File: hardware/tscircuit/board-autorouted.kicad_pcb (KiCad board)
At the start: 4 copper layers, 80 x 175 mm, 174 parts, among them SW1 10mΩ, SW11 10mΩ, SW12 10mΩ, SW13 10mΩ

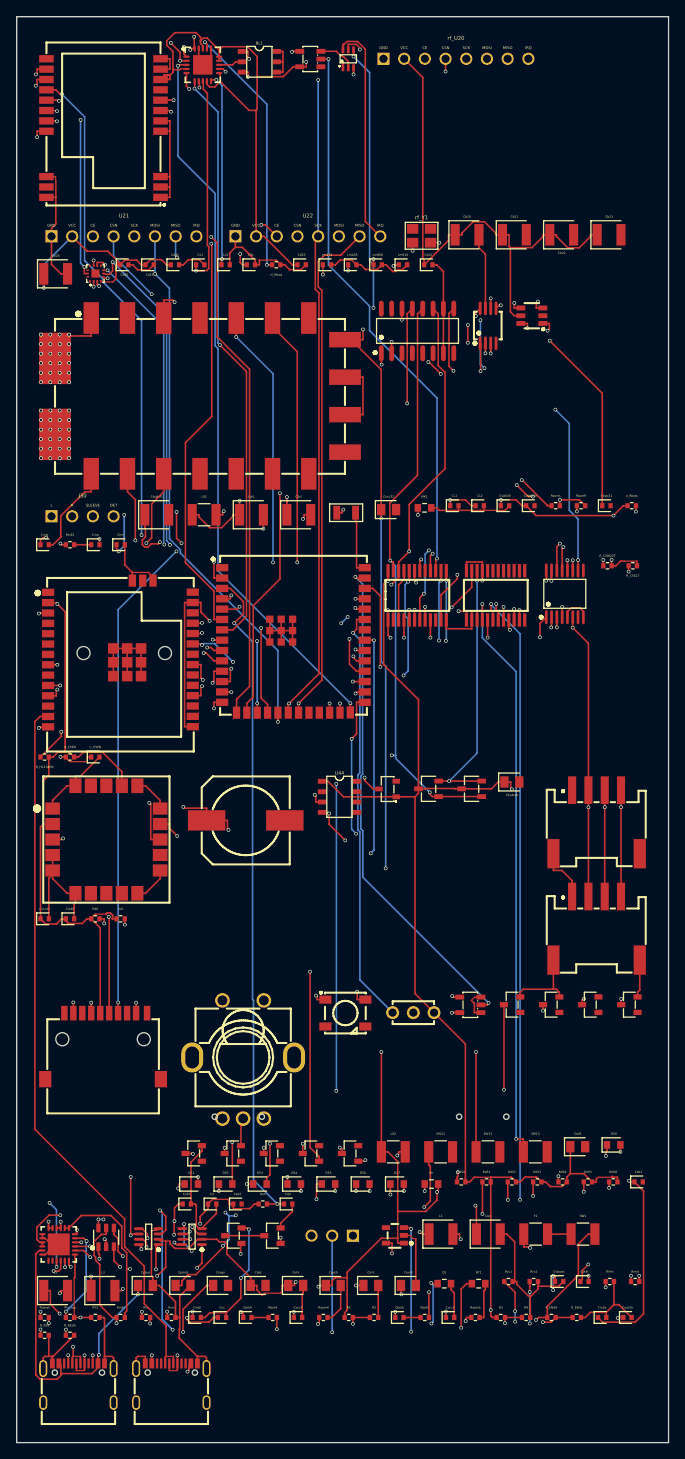
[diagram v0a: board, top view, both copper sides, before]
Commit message: hardware: near-complete auto-route (424/425 nets)
Two-tool pipeline: Freerouting routes signals + RF, then
KiCadRoutingTools plane-finalize welds GND pads to the In1 plane.
Result: 424/425 connections on 4 layers, 3304 segments + 715 vias over
a filled GND plane, only 1 net (encoder B) + 4 DRC clearance nits left.
RF traces still want an impedance/coplanar hand-redo. Supersedes the
Freerouting-only draft in board-autorouted.kicad_pcb.

Co-Authored-By: Claude Opus 4.8 <noreply@anthropic.com>
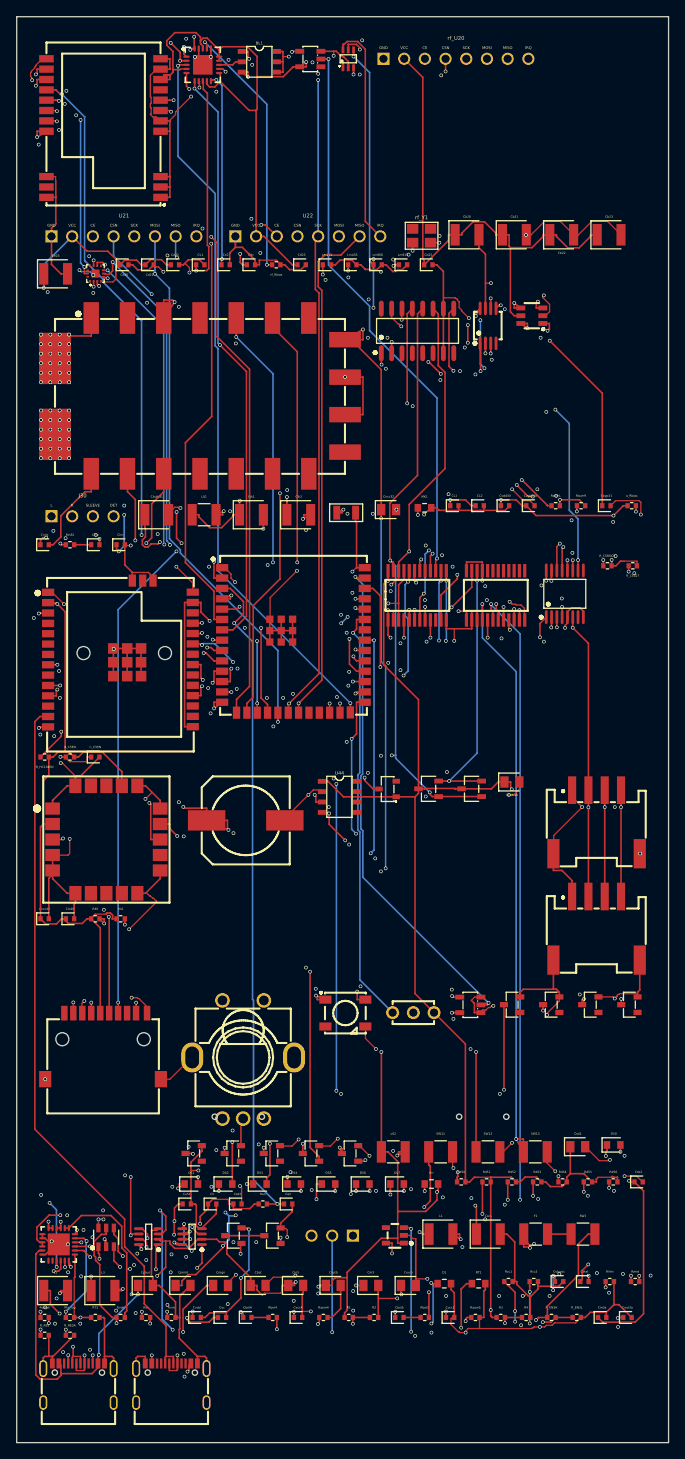
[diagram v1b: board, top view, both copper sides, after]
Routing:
- net GND: track 373.1 -> 581.2 mm, vias 48 -> 306
- net V5: track 342.5 -> 347.3 mm
- net V3V3: track 676.9 -> 680.0 mm
- net V_BCKP: track 47.8 -> 50.8 mm
- net SA_AF: track 53.8 -> 56.1 mm
- net SPK_M: track 46.0 -> 48.1 mm
- net I2C_SDA: track 244.4 -> 246.4 mm
- net .BT1 > .P_PLUS to .F1 > .pin1: track 25.0 -> 26.8 mm
- net PTT_BTN: track 71.8 -> 73.6 mm
- net LoRa_NSS: track 114.9 -> 116.2 mm
- net USB_DP_S3: track 101.3 -> 102.5 mm
- net C5LINK_SCK: track 25.4 -> 26.5 mm
- net SW: track 90.9 -> 92.0 mm
- net .Cjk2 > .pin2 to .J30 > .R: track 30.4 -> 31.5 mm
- net .LS2 > .pin2 to .Q57 > .C: track 15.6 -> 16.7 mm
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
